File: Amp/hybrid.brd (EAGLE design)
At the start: 172.7 x 137.2 mm, 137 parts, among them IC1 TL071P, IC2 TL071P, IC3 LM317MABT, IC4 LM317MABT, J1 NRJ3HF-1, K1 UA2-12NJ, Q1 KSP06KINKED, Q10 BD139, Q11 KSP06KINKED, Q12 BC560KINKED, Q13 BC560KINKED, Q14 BC560KINKED, Q15 BC556KINKED, Q16 BC550KINKED, Q17 BC550KINKED, Q18 BC560KINKED, Q19 BD140, Q2 BC560KINKED, Q20 BD139, Q21 KSP43, Q22 KSP43, Q23 BC546KINKED, Q3 BC560KINKED, Q4 BC560KINKED, Q5 BC556KINKED, Q6 BC550KINKED, Q7 BC550KINKED, Q8 BC560KINKED, Q9 BD140, U1 TL7700DIP-8

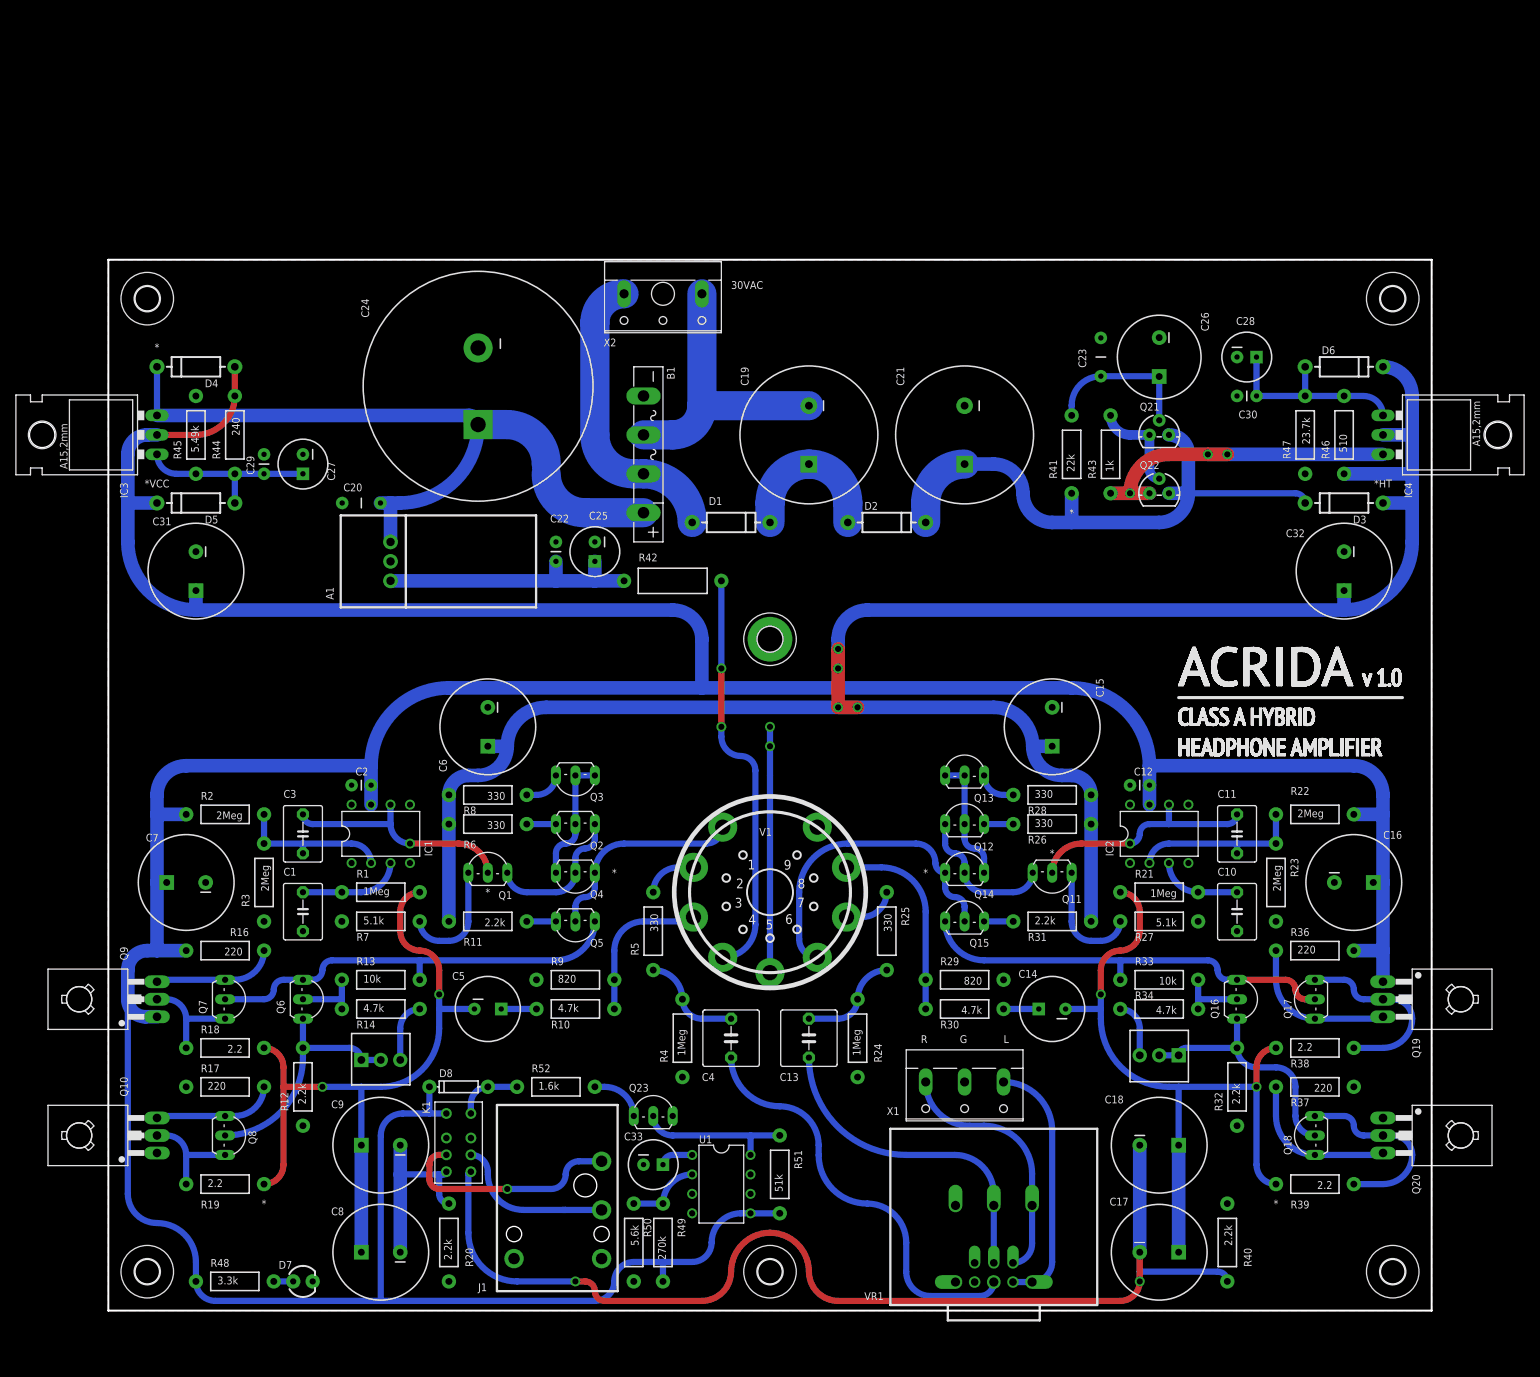
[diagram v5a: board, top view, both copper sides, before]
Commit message: Capacitors polarity was reversed
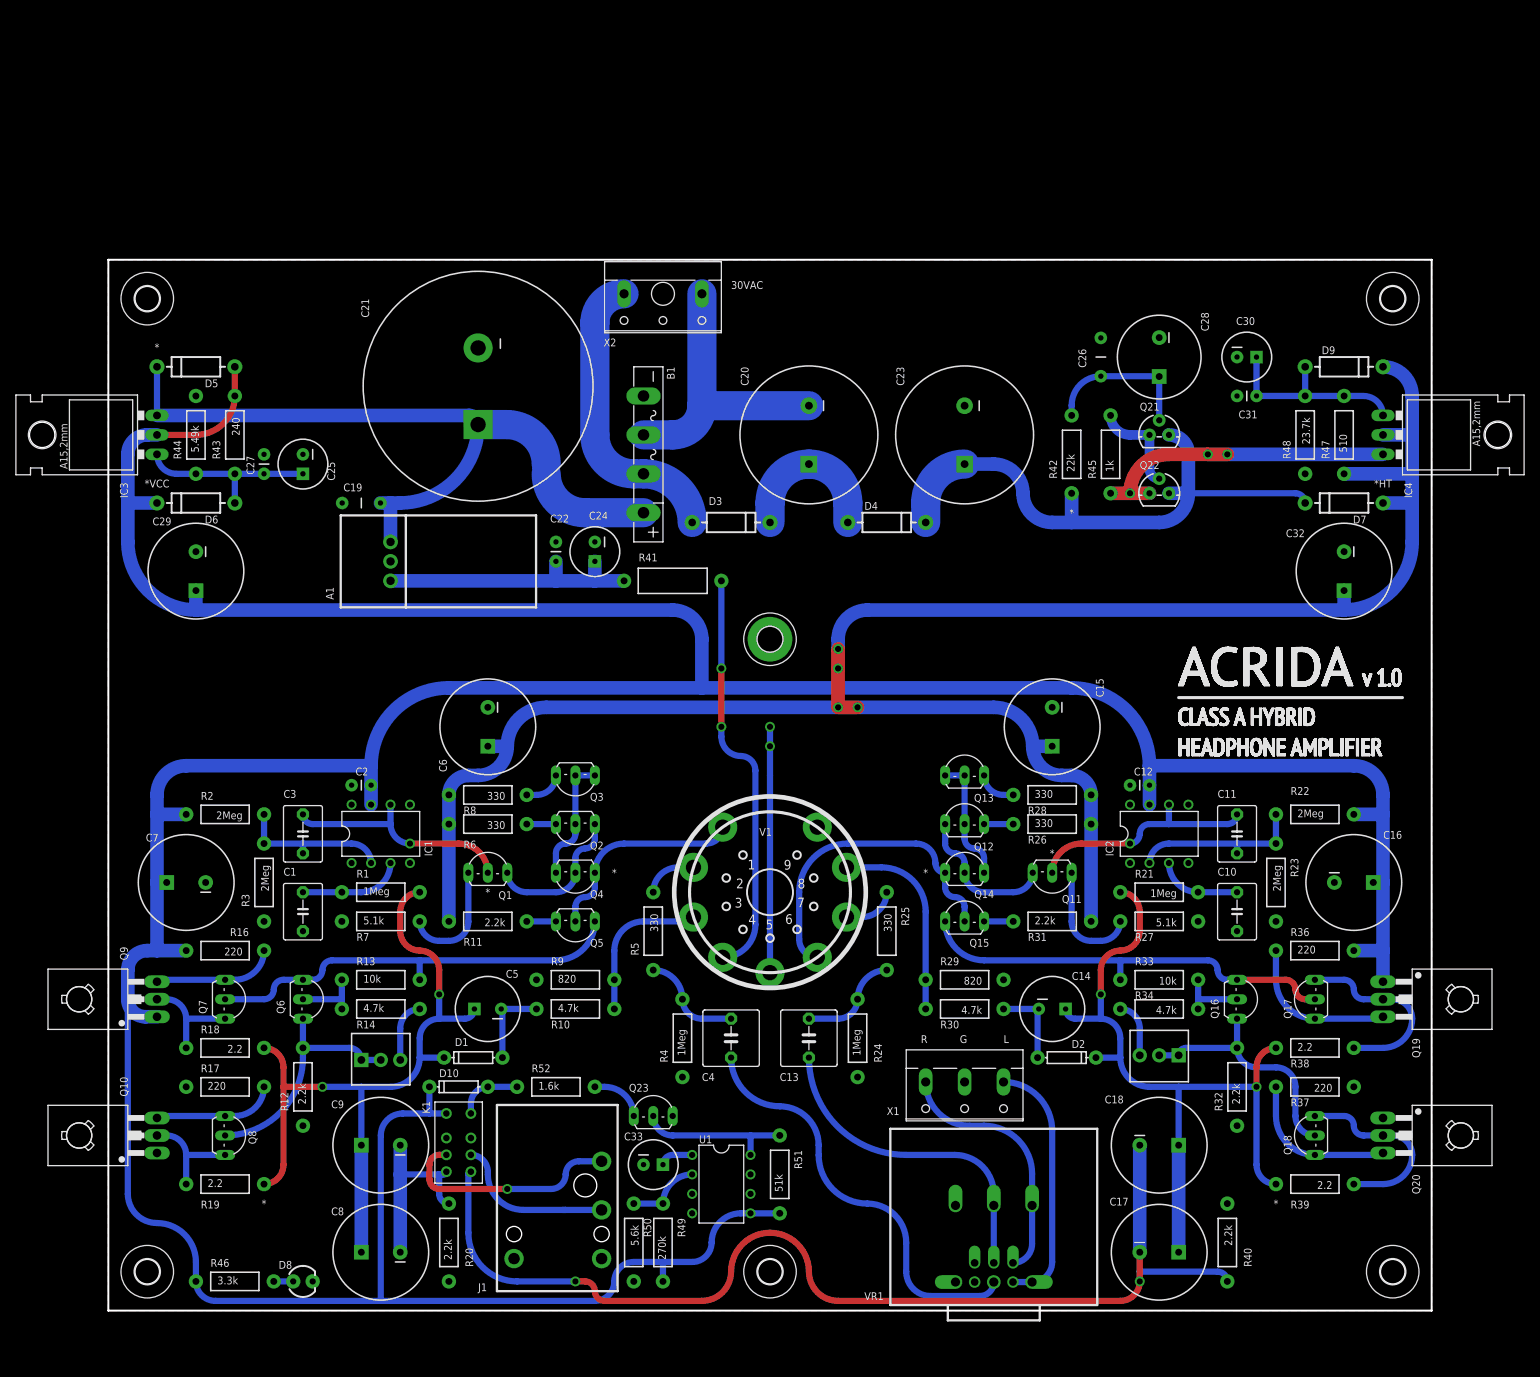
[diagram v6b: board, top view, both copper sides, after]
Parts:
- added D10: 1N4148, my:DIODE-1N4148
- added D9: (no value), SparkFun-DiscreteSemi:DIODE-1N4001
- C19: value 470uF -> 1uF; device my-cap:CPOL-RADIAL-18/7.5 -> SparkFun-Capacitors:CAP-PTH-5MM
- C20, C23: value 1uF -> 470uF; device SparkFun-Capacitors:CAP-PTH-5MM -> my-cap:CPOL-RADIAL-18/7.5
- C21: value 470uF -> 4700uF; device my-cap:CPOL-RADIAL-18/7.5 -> my-cap:CPOL-SNAPIN-30/10
- C24: value 4700uF -> 100uF; device my-cap:CPOL-SNAPIN-30/10 -> my-cap:CPOL-RADIAL-6.5/2.5
- C25: value 100uF -> 10uF
- C26: value 10uF -> 1uF; device my-cap:CPOL-RADIAL-12/5 -> SparkFun-Capacitors:CAP-PTH-5MM
- C27: value 10uF -> 1uF; device my-cap:CPOL-RADIAL-6.5/2.5 -> SparkFun-Capacitors:CAP-PTH-SMALL
- C28: device my-cap:CPOL-RADIAL-6.5/2.5 -> my-cap:CPOL-RADIAL-12/5
- C29: value 1uF -> 100uF; device SparkFun-Capacitors:CAP-PTH-SMALL -> my-cap:CPOL-RADIAL-12.5/5
- C30: value 1uF -> 10uF; device SparkFun-Capacitors:CAP-PTH-SMALL -> my-cap:CPOL-RADIAL-6.5/2.5
- C31: value 100uF -> 1uF; device my-cap:CPOL-RADIAL-12.5/5 -> SparkFun-Capacitors:CAP-PTH-SMALL
- C33: value 10uF -> 100uF
- D1, D2: value (none) -> 1N4148; device SparkFun-DiscreteSemi:DIODE-1N4001 -> my:DIODE-1N4148
- D7: device SparkFun-LED:LED3MM -> SparkFun-DiscreteSemi:DIODE-1N4001
- D8: device SparkFun-DiscreteSemi:DIODE-1N4148-KIT -> SparkFun-LED:LED3MM
- R41: value 22k -> 0.51; device SparkFun-Resistors:AXIAL-0.4 -> my-res:AXIAL-0.5
- R42: value 0.51 -> 22k; device my-res:AXIAL-0.5 -> SparkFun-Resistors:AXIAL-0.4
- R43: value 1k -> 240
- R44: value 240 -> 5.49k
- R45: value 5.49k -> 1k
- R46: value 510 -> 3.3k
- R47: value 23.7k -> 510
- R48: value 3.3k -> 23.7k
- moved R46 182.1 mm to (16.5, 3.81), turned to 0 degrees
- moved R48 178.1 mm to (156.2, 114.3), turned to 270 degrees
- moved D7 169.7 mm to (161.3, 105.4), turned to 180 degrees
- moved D6 150.9 mm to (11.4, 105.4), turned to 180 degrees
- moved C31 140.3 mm to (149.9, 119.4), turned to 180 degrees
- moved R45 119.4 mm to (130.8, 111.8)
- moved R43 114.3 mm to (16.5, 114.3), turned to 270 degrees
- moved D4 92.4 mm to (101.6, 102.9), turned to 0 degrees
- moved D3 80.1 mm to (81.3, 102.9), turned to 0 degrees
- moved D1 77.5 mm to (47.6, 33.0), turned to 180 degrees
- moved D2 73.7 mm to (125.1, 33.0)
- moved C21 63.8 mm to (48.3, 120.7)
- moved C19 59.1 mm to (33.0, 105.4), turned to 180 degrees
- moved C20 59.1 mm to (91.4, 114.3), turned to 270 degrees
- moved R41 54.6 mm to (73.7, 95.2), turned to 0 degrees
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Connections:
- net +6.3FIL: now also R41.P$2; no longer R42.P$2
- net +LV: now also C19.1, C21.1, D5.C; no longer C20.1, C24.1, D4.C
- net AC_1: now also D3.A; no longer D1.A
- net AC_2: now also C20.2; no longer C19.2
- net FB_L: now also C5.1, D1.C; no longer C5.2
- net FB_R: now also C14.1, D2.C; no longer C14.2
- net GND: now also C19.2, C26.2, C28.-, C29.-, C31.2, D8.K, R44.P$2, R48.P$2; no longer C20.2, C26.-, C28.2, C29.2, C31.-, D7.K, R45.P$2, R47.P$2
- net HT: now also D7.A, D9.C, R47.P$1; no longer D3.A, D6.C, R46.P$1
- net N$18: now also R45.P$2; no longer R43.P$2
- net N$19: now also C14.2, D2.A; no longer C14.1
- net N$30: now also C25.1, D6.A, R43.P$2, R44.P$1; no longer C29.1, D5.A, R44.P$2, R45.P$1
- net N$31: now also C20.1, D3.C, D4.A; no longer C19.1, D1.C, D2.A
- net N$32: now also C24.1, R41.P$1; no longer C25.1, R42.P$1
- net N$33: now also C23.1, D4.C, D7.C, R42.P$1; no longer C21.1, D2.C, D3.C, R41.P$1
- net N$34: now also C26.1, C28.+, R42.P$2; no longer C23.1, C26.+, R41.P$2
- net N$36: now also C31.1, D9.A, R47.P$2, R48.P$1; no longer C28.1, D6.A, R46.P$2, R47.P$1
- net N$37: now also R45.P$1; no longer R43.P$1
- net N$4: now also C5.2, D1.A; no longer C5.1
- net N$46: now also D8.A, R46.P$2; no longer D7.A, R48.P$2
- net N$49: now also D10.A; no longer D8.A
- net VCC: now also C29.+, D10.C, D5.A, D6.C, R43.P$1, R46.P$1; no longer C31.+, D4.A, D5.C, D8.C, R44.P$1, R48.P$1
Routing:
- net N$4: track 4.60 -> 11.0 mm
- net N$19: track 4.60 -> 11.0 mm
- net FB_R: track 89.7 -> 94.9 mm
- net FB_L: track 90.5 -> 94.9 mm

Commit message: Adjust some components a bit
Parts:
- moved R51 1.27 mm to (88.9, 17.8)
- moved C33 1.27 mm to (72.4, 19.1)
- moved Q23 1.27 mm to (72.4, 26.7)
- moved R49 1.27 mm to (73.7, 8.89)
- moved R50 1.27 mm to (69.8, 8.89)
- moved U1 1.27 mm to (81.3, 16.5)
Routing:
- net N$50: track 6.66 -> 7.93 mm
- net VCC: track 542.8 -> 544.1 mm
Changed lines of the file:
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@@
 <attribute name="VALUE" x="59.944" y="98.044" size="1.016" layer="27" ratio="19" rot="R90"/>
 </element>
-<element name="U1" library="my-ic" package="DIL08" value="TL7700DIP-8" x="80.01" y="16.51" smashed="yes" rot="R270">
-<attribute name="NAME" x="77.089" y="21.844" size="1.016" layer="25" ratio="19"/>
-<attribute name="VALUE" x="79.375" y="20.066" size="1.016" layer="27" ratio="19" rot="R270"/>
-</element>
-<element name="C33" library="my-cap" package="CPOL-RADIAL-6.5/2.5" value="100uF" x="71.12" y="19.05" smashed="yes">
-<attribute name="NAME" x="67.31" y="22.225" size="1.016" layer="25" ratio="19"/>
-<attribute name="VALUE" x="69.215" y="15.367" size="1.016" layer="27" ratio="19"/>
-</element>
-<element name="R49" library="SparkFun-Resistors" package="AXIAL-0.4" value="270k" x="72.39" y="8.89" smashed="yes" rot="R90">
-<attribute name="NAME" x="74.295" y="12.065" size="1.016" layer="25" font="vector" ratio="19" rot="R270"/>
-<attribute name="VALUE" x="72.771" y="6.604" size="1.016" layer="21" font="vector" ratio="19" rot="R90"/>
-</element>
-<element name="R50" library="SparkFun-Resistors" package="AXIAL-0.4" value="5.6k" x="68.58" y="8.89" smashed="yes" rot="R270">
-<attribute name="NAME" x="69.85" y="12.065" size="1.016" layer="25" font="vector" ratio="19" rot="R270"/>
-<attribute name="VALUE" x="68.199" y="11.176" size="1.016" layer="21" font="vector" ratio="19" rot="R270"/>
-</element>
-<element name="Q23" library="my-tran" package="TO92-BENT" value="BC546KINKED" x="71.12" y="26.67" smashed="yes">
-<attribute name="NAME" x="67.945" y="28.575" size="1.016" layer="25" ratio="19"/>
-<attribute name="VALUE" x="68.58" y="22.098" size="1.016" layer="27" ratio="19"/>
-</element>
-<element name="R51" library="SparkFun-Resistors" package="AXIAL-0.4" value="51k" x="87.63" y="17.78" smashed="yes" rot="R90">
-<attribute name="NAME" x="89.535" y="20.955" size="1.016" layer="25" font="vector" ratio="19" rot="R270"/>
-<attribute name="VALUE" x="88.011" y="15.494" size="1.016" layer="21" font="vector" ratio="19" rot="R90"/>
+<element name="U1" library="my-ic" package="DIL08" value="TL7700DIP-8" x="81.28" y="16.51" smashed="yes" rot="R270">
+<attribute name="NAME" x="78.359" y="21.844" size="1.016" layer="25" ratio="19"/>
+<attribute name="VALUE" x="80.645" y="20.066" size="1.016" layer="27" ratio="19" rot="R270"/>
+</element>
+<element name="C33" library="my-cap" package="CPOL-RADIAL-6.5/2.5" value="100uF" x="72.39" y="19.05" smashed="yes">
+<attribute name="NAME" x="68.58" y="22.225" size="1.016" layer="25" ratio="19"/>
+<attribute name="VALUE" x="70.485" y="15.367" size="1.016" layer="27" ratio="19"/>
+</element>
+<element name="R49" library="SparkFun-Resistors" package="AXIAL-0.4" value="270k" x="73.66" y="8.89" smashed="yes" rot="R90">
+<attribute name="NAME" x="75.565" y="12.065" size="1.016" layer="25" font="vector" ratio="19" rot="R270"/>
+<attribute name="VALUE" x="74.041" y="6.604" size="1.016" layer="21" font="vector" ratio="19" rot="R90"/>
+</element>
+<element name="R50" library="SparkFun-Resistors" package="AXIAL-0.4" value="5.6k" x="69.85" y="8.89" smashed="yes" rot="R270">
+<attribute name="NAME" x="71.12" y="12.065" size="1.016" layer="25" font="vector" ratio="19" rot="R270"/>
+<attribute name="VALUE" x="69.469" y="11.176" size="1.016" layer="21" font="vector" ratio="19" rot="R270"/>
+</element>
+<element name="Q23" library="my-tran" package="TO92-BENT" value="BC546KINKED" x="72.39" y="26.67" smashed="yes">
+<attribute name="NAME" x="69.215" y="28.575" size="1.016" layer="25" ratio="19"/>
+<attribute name="VALUE" x="69.85" y="22.098" size="1.016" layer="27" ratio="19"/>
+</element>
+<element name="R51" library="SparkFun-Resistors" package="AXIAL-0.4" value="51k" x="88.9" y="17.78" smashed="yes" rot="R90">
+<attribute name="NAME" x="90.805" y="20.955" size="1.016" layer="25" font="vector" ratio="19" rot="R270"/>
+<attribute name="VALUE" x="89.281" y="15.494" size="1.016" layer="21" font="vector" ratio="19" rot="R90"/>
 </element>
 <element name="D10" library="my" package="DIODE-1N4148" value="1N4148" x="45.72" y="29.21" smashed="yes" rot="R180">
@@
 <wire x1="11.43" y1="3.81" x2="13.97" y2="1.27" width="0.8128" layer="16" curve="90"/>
 <wire x1="13.97" y1="1.27" x2="35.56" y2="1.27" width="0.8128" layer="16"/>
-<wire x1="83.82" y1="12.7" x2="87.63" y2="12.7" width="0.8128" layer="16"/>
+<wire x1="85.09" y1="12.7" x2="88.9" y2="12.7" width="0.8128" layer="16"/>
 <wire x1="41.91" y1="25.73" x2="44.12" y2="25.73" width="0.8128" layer="16"/>
 <wire x1="41.91" y1="25.73" x2="38.43" y2="25.73" width="0.8128" layer="16"/>
@@
 <wire x1="35.56" y1="22.86" x2="35.56" y2="1.27" width="0.8128" layer="16"/>
 <wire x1="41.91" y1="29.21" x2="41.91" y2="25.73" width="0.8128" layer="16"/>
-<wire x1="35.56" y1="1.27" x2="63.5" y2="1.27" width="0.8128" layer="16"/>
-<wire x1="63.5" y1="1.27" x2="66.04" y2="3.81" width="0.8128" layer="16" curve="90"/>
-<wire x1="66.04" y1="3.81" x2="68.58" y2="6.35" width="0.8128" layer="16" curve="-90"/>
-<wire x1="68.58" y1="6.35" x2="72.39" y2="6.35" width="0.8128" layer="16"/>
-<wire x1="72.39" y1="3.81" x2="72.39" y2="6.35" width="0.8128" layer="16"/>
-<wire x1="72.39" y1="6.35" x2="76.2" y2="6.35" width="0.8128" layer="16"/>
-<wire x1="76.2" y1="6.35" x2="78.74" y2="8.89" width="0.8128" layer="16" curve="90"/>
-<wire x1="78.74" y1="8.89" x2="82.55" y2="12.7" width="0.8128" layer="16" curve="-90"/>
-<wire x1="82.55" y1="12.7" x2="83.82" y2="12.7" width="0.8128" layer="16"/>
+<wire x1="69.85" y1="6.35" x2="73.66" y2="6.35" width="0.8128" layer="16"/>
+<wire x1="73.66" y1="3.81" x2="73.66" y2="6.35" width="0.8128" layer="16"/>
+<wire x1="73.66" y1="6.35" x2="77.47" y2="6.35" width="0.8128" layer="16"/>
+<wire x1="77.47" y1="6.35" x2="80.01" y2="8.89" width="0.8128" layer="16" curve="90"/>
+<wire x1="80.01" y1="8.89" x2="83.82" y2="12.7" width="0.8128" layer="16" curve="-90"/>
+<wire x1="83.82" y1="12.7" x2="85.09" y2="12.7" width="0.8128" layer="16"/>
 <wire x1="6.35" y1="114.3" x2="11.43" y2="114.3" width="0.8128" layer="1"/>
 <wire x1="11.43" y1="114.3" x2="16.51" y2="119.38" width="0.8128" layer="1" curve="90"/>
 <wire x1="16.51" y1="119.38" x2="16.51" y2="123.19" width="0.8128" layer="1"/>
+<wire x1="64.77" y1="1.27" x2="67.31" y2="3.81" width="0.8128" layer="16" curve="90"/>
+<wire x1="67.31" y1="3.81" x2="69.85" y2="6.35" width="0.8128" layer="16" curve="-90"/>
+<wire x1="35.56" y1="1.27" x2="64.77" y2="1.27" width="0.8128" layer="16"/>
 </signal>
 <signal name="OUT_L" class="1">
@@
 <contactref element="U1" pad="1"/>
 <contactref element="C33" pad="1"/>
-<wire x1="72.39" y1="19.05" x2="73.66" y2="20.32" width="0.8128" layer="16" curve="-90"/>
-<wire x1="73.66" y1="20.32" x2="76.2" y2="20.32" width="0.8128" layer="16"/>
+<wire x1="73.66" y1="19.05" x2="74.93" y2="20.32" width="0.8128" layer="16" curve="-90"/>
+<wire x1="74.93" y1="20.32" x2="77.47" y2="20.32" width="0.8128" layer="16"/>
 </signal>
 <signal name="N$45">
@@
 <contactref element="R49" pad="P$2"/>
 <contactref element="U1" pad="2"/>
-<wire x1="68.58" y1="13.97" x2="72.39" y2="13.97" width="0.8128" layer="16"/>
-<wire x1="72.39" y1="13.97" x2="76.2" y2="17.78" width="0.8128" layer="16" curve="-90"/>
+<wire x1="69.85" y1="13.97" x2="73.66" y2="13.97" width="0.8128" layer="16"/>
+<wire x1="73.66" y1="13.97" x2="77.47" y2="17.78" width="0.8128" layer="16" curve="-90"/>
 </signal>
 <signal name="N$44">
@@
 <contactref element="U1" pad="8"/>
 <contactref element="R51" pad="P$2"/>
-<wire x1="83.82" y1="22.86" x2="87.63" y2="22.86" width="0.8128" layer="16"/>
-<wire x1="83.82" y1="22.86" x2="73.66" y2="22.86" width="0.8128" layer="16"/>
-<wire x1="73.66" y1="22.86" x2="71.12" y2="25.4" width="0.8128" layer="16" curve="-90"/>
-<wire x1="83.82" y1="20.32" x2="83.82" y2="22.86" width="0.8128" layer="16"/>
+<wire x1="85.09" y1="22.86" x2="88.9" y2="22.86" width="0.8128" layer="16"/>
+<wire x1="85.09" y1="22.86" x2="74.93" y2="22.86" width="0.8128" layer="16"/>
+<wire x1="74.93" y1="22.86" x2="72.39" y2="25.4" width="0.8128" layer="16" curve="-90"/>
+<wire x1="85.09" y1="20.32" x2="85.09" y2="22.86" width="0.8128" layer="16"/>
 </signal>
 <signal name="N$49">
@@
 <contactref element="Q23" pad="1"/>
 <contactref element="R52" pad="P$2"/>
-<wire x1="68.58" y1="25.4" x2="64.77" y2="29.21" width="0.8128" layer="16" curve="90"/>
-<wire x1="64.77" y1="29.21" x2="63.5" y2="29.21" width="0.8128" layer="16"/>
+<wire x1="63.5" y1="29.21" x2="66.04" y2="29.21" width="0.8128" layer="16"/>
+<wire x1="66.04" y1="29.21" x2="69.85" y2="25.4" width="0.8128" layer="16" curve="-90"/>
 </signal>
 <signal name="OUT_L*">
